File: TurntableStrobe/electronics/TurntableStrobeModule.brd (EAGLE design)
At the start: 25.1 x 20.3 mm, 11 parts, among them IC1 TINY25, J1 ISP, Q1 12MHz

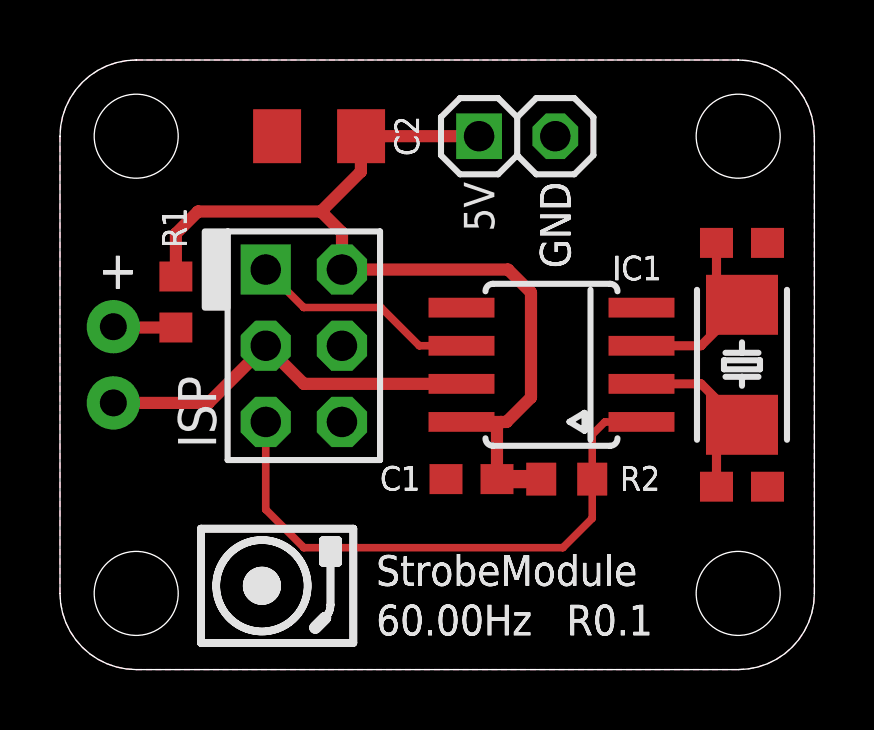
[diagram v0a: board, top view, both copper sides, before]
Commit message: Fixed bug with missing MOSI.
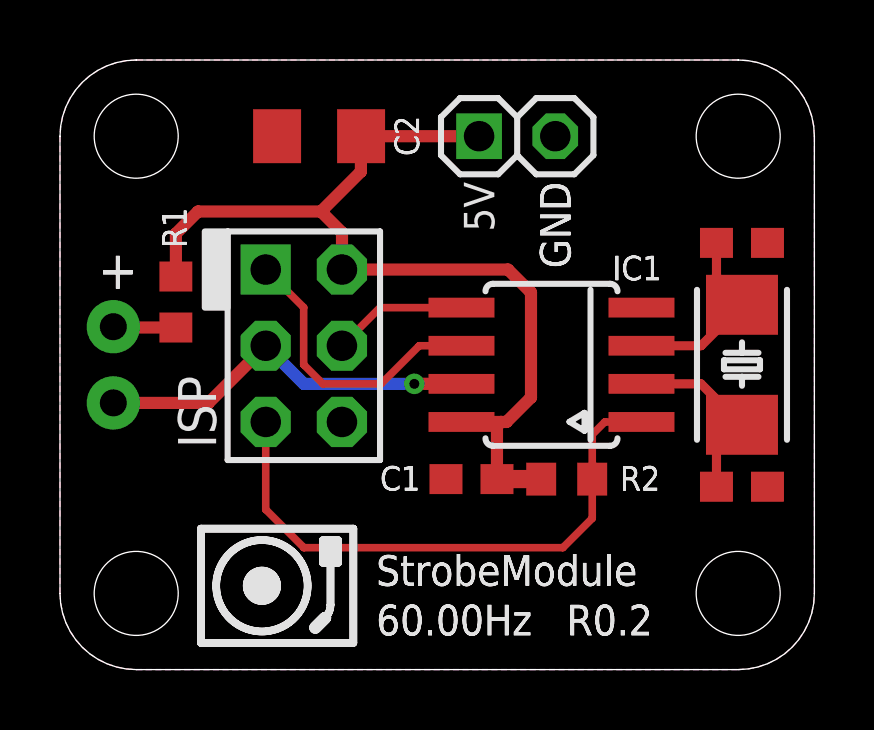
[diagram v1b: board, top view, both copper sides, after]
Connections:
- net PB0: now also IC1.5
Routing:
- net PB0: track 0.00 -> 4.51 mm
- net PB1: track 7.58 -> 9.75 mm
- net PB2: vias 0 -> 1
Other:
- board text added: "R0.2"
- board text removed: "R0.1"
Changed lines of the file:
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@@
 <setting verticaltext="up"/>
 </settings>
-<grid distance="0.01" unitdist="inch" unit="inch" style="lines" multiple="1" display="no" altdistance="0.005" altunitdist="inch" altunit="inch"/>
+<grid distance="0.005" unitdist="inch" unit="inch" style="lines" multiple="1" display="no" altdistance="0.005" altunitdist="inch" altunit="inch"/>
 <layers>
 <layer number="1" name="Top" color="4" fill="1" visible="yes" active="yes"/>
@@
 <layer number="19" name="Unrouted" color="6" fill="1" visible="yes" active="yes"/>
 <layer number="20" name="Dimension" color="15" fill="1" visible="yes" active="yes"/>
-<layer number="21" name="tPlace" color="7" fill="1" visible="no" active="yes"/>
-<layer number="22" name="bPlace" color="7" fill="1" visible="no" active="yes"/>
-<layer number="23" name="tOrigins" color="15" fill="1" visible="no" active="yes"/>
-<layer number="24" name="bOrigins" color="15" fill="1" visible="no" active="yes"/>
-<layer number="25" name="tNames" color="7" fill="1" visible="no" active="yes"/>
-<layer number="26" name="bNames" color="7" fill="1" visible="no" active="yes"/>
-<layer number="27" name="tValues" color="7" fill="1" visible="no" active="yes"/>
-<layer number="28" name="bValues" color="7" fill="1" visible="no" active="yes"/>
+<layer number="21" name="tPlace" color="7" fill="1" visible="yes" active="yes"/>
+<layer number="22" name="bPlace" color="7" fill="1" visible="yes" active="yes"/>
+<layer number="23" name="tOrigins" color="15" fill="1" visible="yes" active="yes"/>
+<layer number="24" name="bOrigins" color="15" fill="1" visible="yes" active="yes"/>
+<layer number="25" name="tNames" color="7" fill="1" visible="yes" active="yes"/>
+<layer number="26" name="bNames" color="7" fill="1" visible="yes" active="yes"/>
+<layer number="27" name="tValues" color="7" fill="1" visible="yes" active="yes"/>
+<layer number="28" name="bValues" color="7" fill="1" visible="yes" active="yes"/>
 <layer number="29" name="tStop" color="7" fill="3" visible="yes" active="yes"/>
 <layer number="30" name="bStop" color="7" fill="6" visible="yes" active="yes"/>
@@
 <vertex x="7.600621875" y="3.150003125"/>
 </polygon>
-<text x="16.891" y="1.143" size="1.016" layer="25" font="vector" ratio="10">R0.1</text>
+<text x="16.891" y="1.143" size="1.016" layer="25" font="vector" ratio="10">R0.2</text>
 <circle x="6.731" y="2.794" radius="1.524" width="0.254" layer="21"/>
 <polygon width="0.254" layer="21">
@@
 </polygon>
 <text x="10.541" y="2.794" size="1.016" layer="121" font="vector" ratio="20">StrobeModule</text>
-<text x="16.891" y="1.143" size="1.016" layer="121" font="vector" ratio="20">R0.1</text>
+<text x="16.891" y="1.143" size="1.016" layer="121" font="vector" ratio="20">R0.2</text>
 <text x="10.541" y="1.143" size="1.016" layer="121" font="vector" ratio="20">60.00Hz</text>
 <text x="16.002" y="16.256" size="1.016" layer="121" font="vector" ratio="20" rot="R270">GND</text>
@@
 <signal name="PB0">
 <contactref element="J1" pad="4"/>
+<contactref element="IC1" pad="5"/>
+<wire x1="13.383" y1="12.065" x2="10.668" y2="12.065" width="0.254" layer="1"/>
+<wire x1="10.668" y1="12.065" x2="9.398" y2="10.795" width="0.254" layer="1"/>
 </signal>
 <signal name="PB1">
@@
 <contactref element="J1" pad="1"/>
 <wire x1="13.383" y1="10.795" x2="11.975" y2="10.795" width="0.254" layer="1"/>
-<wire x1="11.975" y1="10.795" x2="10.7" y2="12.07" width="0.254" layer="1"/>
-<wire x1="10.7" y1="12.07" x2="8.123" y2="12.07" width="0.254" layer="1"/>
 <wire x1="8.123" y1="12.07" x2="6.858" y2="13.335" width="0.254" layer="1"/>
+<wire x1="8.123" y1="12.07" x2="8.123" y2="10.165" width="0.254" layer="1"/>
+<wire x1="8.123" y1="10.165" x2="8.763" y2="9.525" width="0.254" layer="1"/>
+<wire x1="8.763" y1="9.525" x2="10.705" y2="9.525" width="0.254" layer="1"/>
+<wire x1="10.705" y1="9.525" x2="11.975" y2="10.795" width="0.254" layer="1"/>
 </signal>
 <signal name="PB2">
@@
 <contactref element="J1" pad="3"/>
 <contactref element="LED1" pad="C"/>
-<wire x1="13.383" y1="9.525" x2="8.128" y2="9.525" width="0.4064" layer="1"/>
-<wire x1="8.128" y1="9.525" x2="6.858" y2="10.795" width="0.4064" layer="1"/>
 <wire x1="1.778" y1="8.89" x2="4.953" y2="8.89" width="0.4064" layer="1"/>
 <wire x1="4.953" y1="8.89" x2="6.858" y2="10.795" width="0.4064" layer="1"/>
+<wire x1="13.383" y1="9.525" x2="11.811" y2="9.525" width="0.4064" layer="1"/>
+<via x="11.811" y="9.525" extent="1-16" drill="0.3302"/>
+<wire x1="11.811" y1="9.525" x2="8.128" y2="9.525" width="0.4064" layer="16"/>
+<wire x1="8.128" y1="9.525" x2="6.858" y2="10.795" width="0.4064" layer="16"/>
 </signal>
 <signal name="PB4">

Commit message: Removed hardware directory. Updated boards. Modified timing calcs spreadsheet.
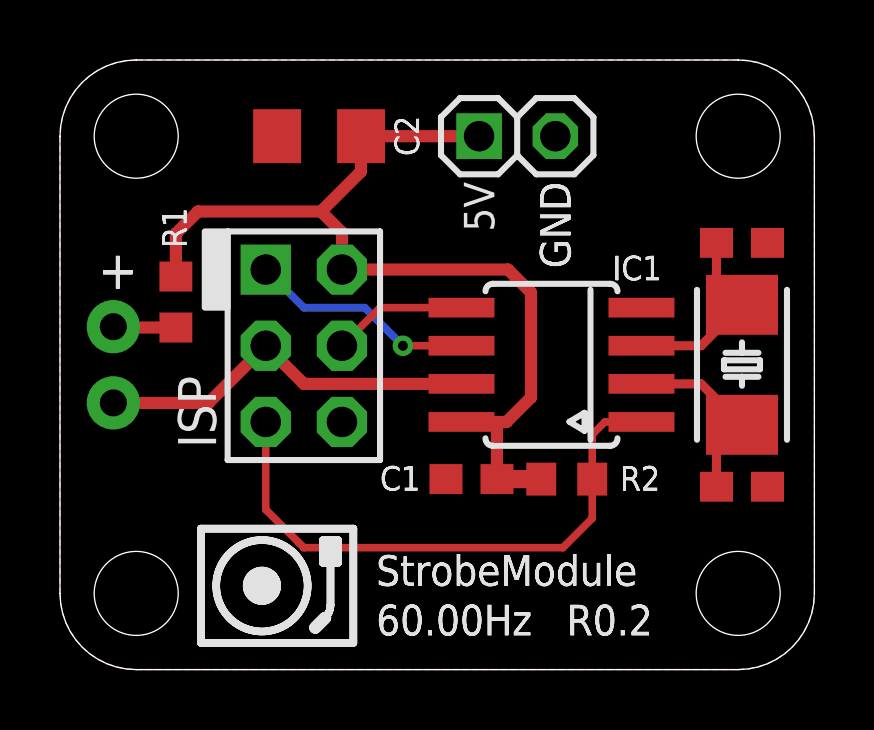
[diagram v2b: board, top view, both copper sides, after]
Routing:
- net PB1: track 9.75 -> 7.58 mm, vias 0 -> 1
- net PB2: vias 1 -> 0
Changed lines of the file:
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@@
 <layer number="19" name="Unrouted" color="6" fill="1" visible="yes" active="yes"/>
 <layer number="20" name="Dimension" color="15" fill="1" visible="yes" active="yes"/>
-<layer number="21" name="tPlace" color="7" fill="1" visible="yes" active="yes"/>
-<layer number="22" name="bPlace" color="7" fill="1" visible="yes" active="yes"/>
-<layer number="23" name="tOrigins" color="15" fill="1" visible="yes" active="yes"/>
-<layer number="24" name="bOrigins" color="15" fill="1" visible="yes" active="yes"/>
-<layer number="25" name="tNames" color="7" fill="1" visible="yes" active="yes"/>
-<layer number="26" name="bNames" color="7" fill="1" visible="yes" active="yes"/>
-<layer number="27" name="tValues" color="7" fill="1" visible="yes" active="yes"/>
-<layer number="28" name="bValues" color="7" fill="1" visible="yes" active="yes"/>
+<layer number="21" name="tPlace" color="7" fill="1" visible="no" active="yes"/>
+<layer number="22" name="bPlace" color="7" fill="1" visible="no" active="yes"/>
+<layer number="23" name="tOrigins" color="15" fill="1" visible="no" active="yes"/>
+<layer number="24" name="bOrigins" color="15" fill="1" visible="no" active="yes"/>
+<layer number="25" name="tNames" color="7" fill="1" visible="no" active="yes"/>
+<layer number="26" name="bNames" color="7" fill="1" visible="no" active="yes"/>
+<layer number="27" name="tValues" color="7" fill="1" visible="no" active="yes"/>
+<layer number="28" name="bValues" color="7" fill="1" visible="no" active="yes"/>
 <layer number="29" name="tStop" color="7" fill="3" visible="yes" active="yes"/>
 <layer number="30" name="bStop" color="7" fill="6" visible="yes" active="yes"/>
@@
 <contactref element="IC1" pad="6"/>
 <contactref element="J1" pad="1"/>
-<wire x1="13.383" y1="10.795" x2="11.975" y2="10.795" width="0.254" layer="1"/>
-<wire x1="8.123" y1="12.07" x2="6.858" y2="13.335" width="0.254" layer="1"/>
-<wire x1="8.123" y1="12.07" x2="8.123" y2="10.165" width="0.254" layer="1"/>
-<wire x1="8.123" y1="10.165" x2="8.763" y2="9.525" width="0.254" layer="1"/>
-<wire x1="8.763" y1="9.525" x2="10.705" y2="9.525" width="0.254" layer="1"/>
-<wire x1="10.705" y1="9.525" x2="11.975" y2="10.795" width="0.254" layer="1"/>
+<wire x1="13.383" y1="10.795" x2="11.43" y2="10.795" width="0.254" layer="1"/>
+<via x="11.43" y="10.795" extent="1-16" drill="0.3302"/>
+<wire x1="11.43" y1="10.795" x2="10.16" y2="12.065" width="0.254" layer="16"/>
+<wire x1="10.16" y1="12.065" x2="8.128" y2="12.065" width="0.254" layer="16"/>
+<wire x1="8.128" y1="12.065" x2="6.858" y2="13.335" width="0.254" layer="16"/>
 </signal>
 <signal name="PB2">
@@
 <wire x1="1.778" y1="8.89" x2="4.953" y2="8.89" width="0.4064" layer="1"/>
 <wire x1="4.953" y1="8.89" x2="6.858" y2="10.795" width="0.4064" layer="1"/>
-<wire x1="13.383" y1="9.525" x2="11.811" y2="9.525" width="0.4064" layer="1"/>
-<via x="11.811" y="9.525" extent="1-16" drill="0.3302"/>
-<wire x1="11.811" y1="9.525" x2="8.128" y2="9.525" width="0.4064" layer="16"/>
-<wire x1="8.128" y1="9.525" x2="6.858" y2="10.795" width="0.4064" layer="16"/>
+<wire x1="13.383" y1="9.525" x2="8.128" y2="9.525" width="0.4064" layer="1"/>
+<wire x1="8.128" y1="9.525" x2="6.858" y2="10.795" width="0.4064" layer="1"/>
 </signal>
 <signal name="PB4">
